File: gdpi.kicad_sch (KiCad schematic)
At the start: 20 parts, among them J7 HDMI_C_1.3, U1 ECP5U_12_CABGA256, U9 PCA9306DC1

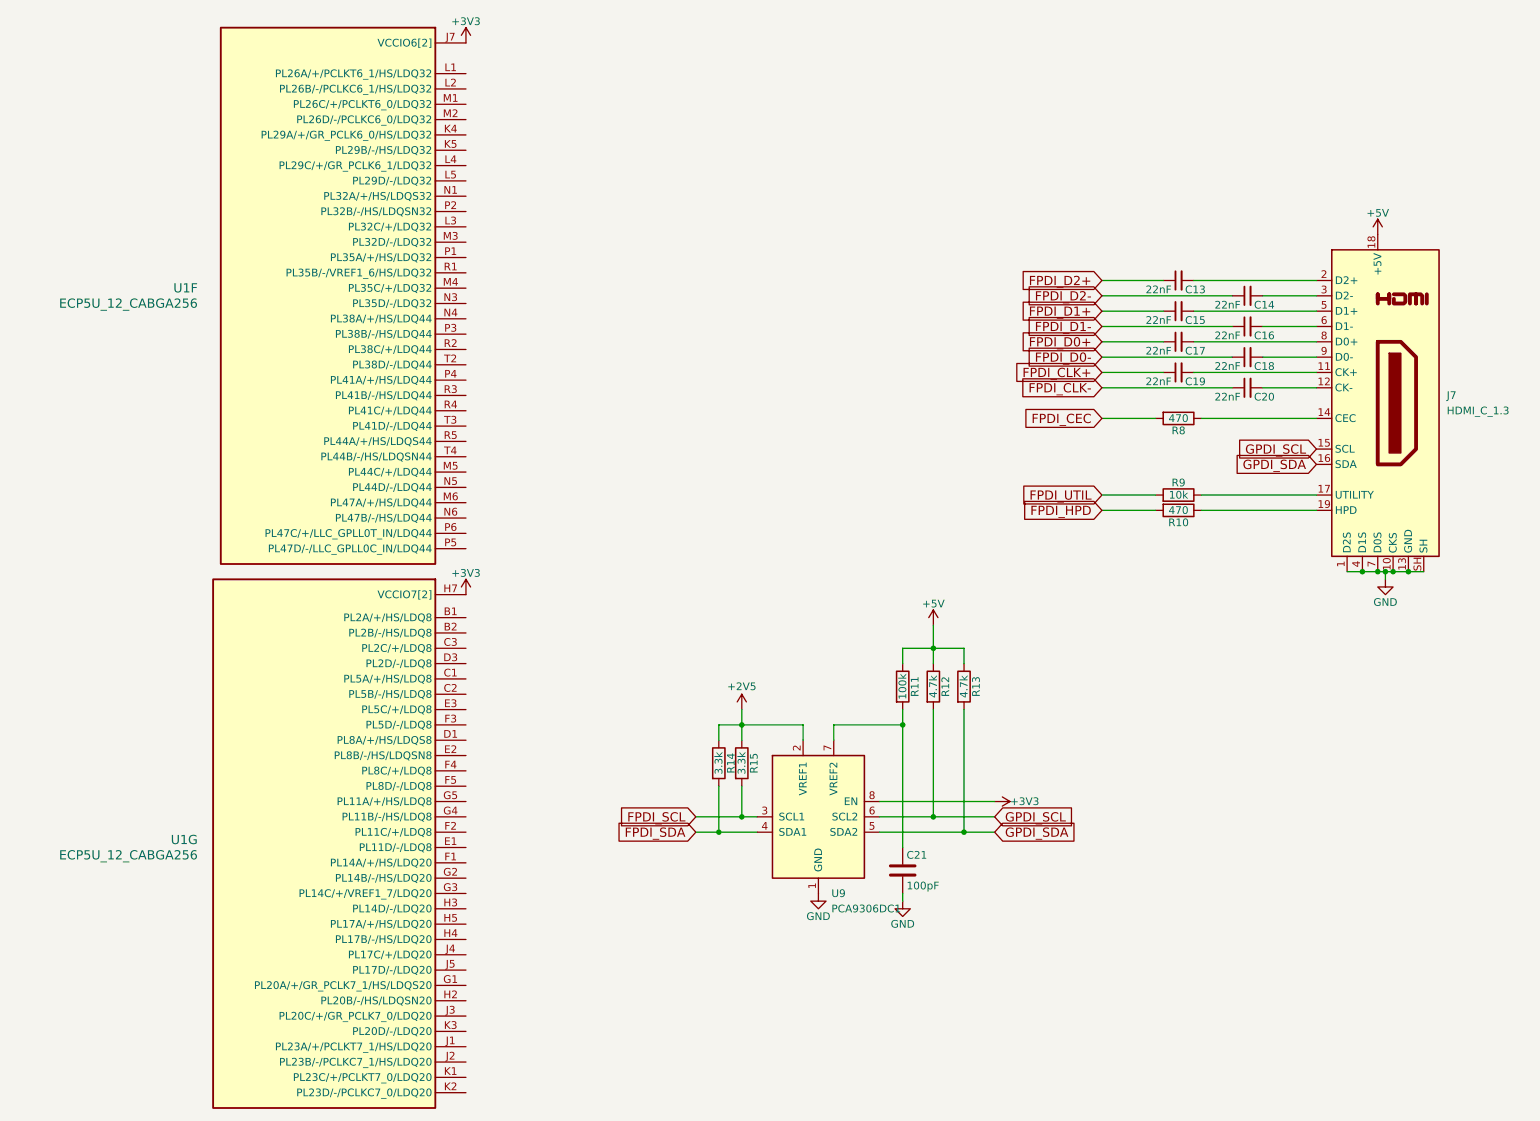
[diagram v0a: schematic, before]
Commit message: Routed HDMI, usb, rotated chip and more
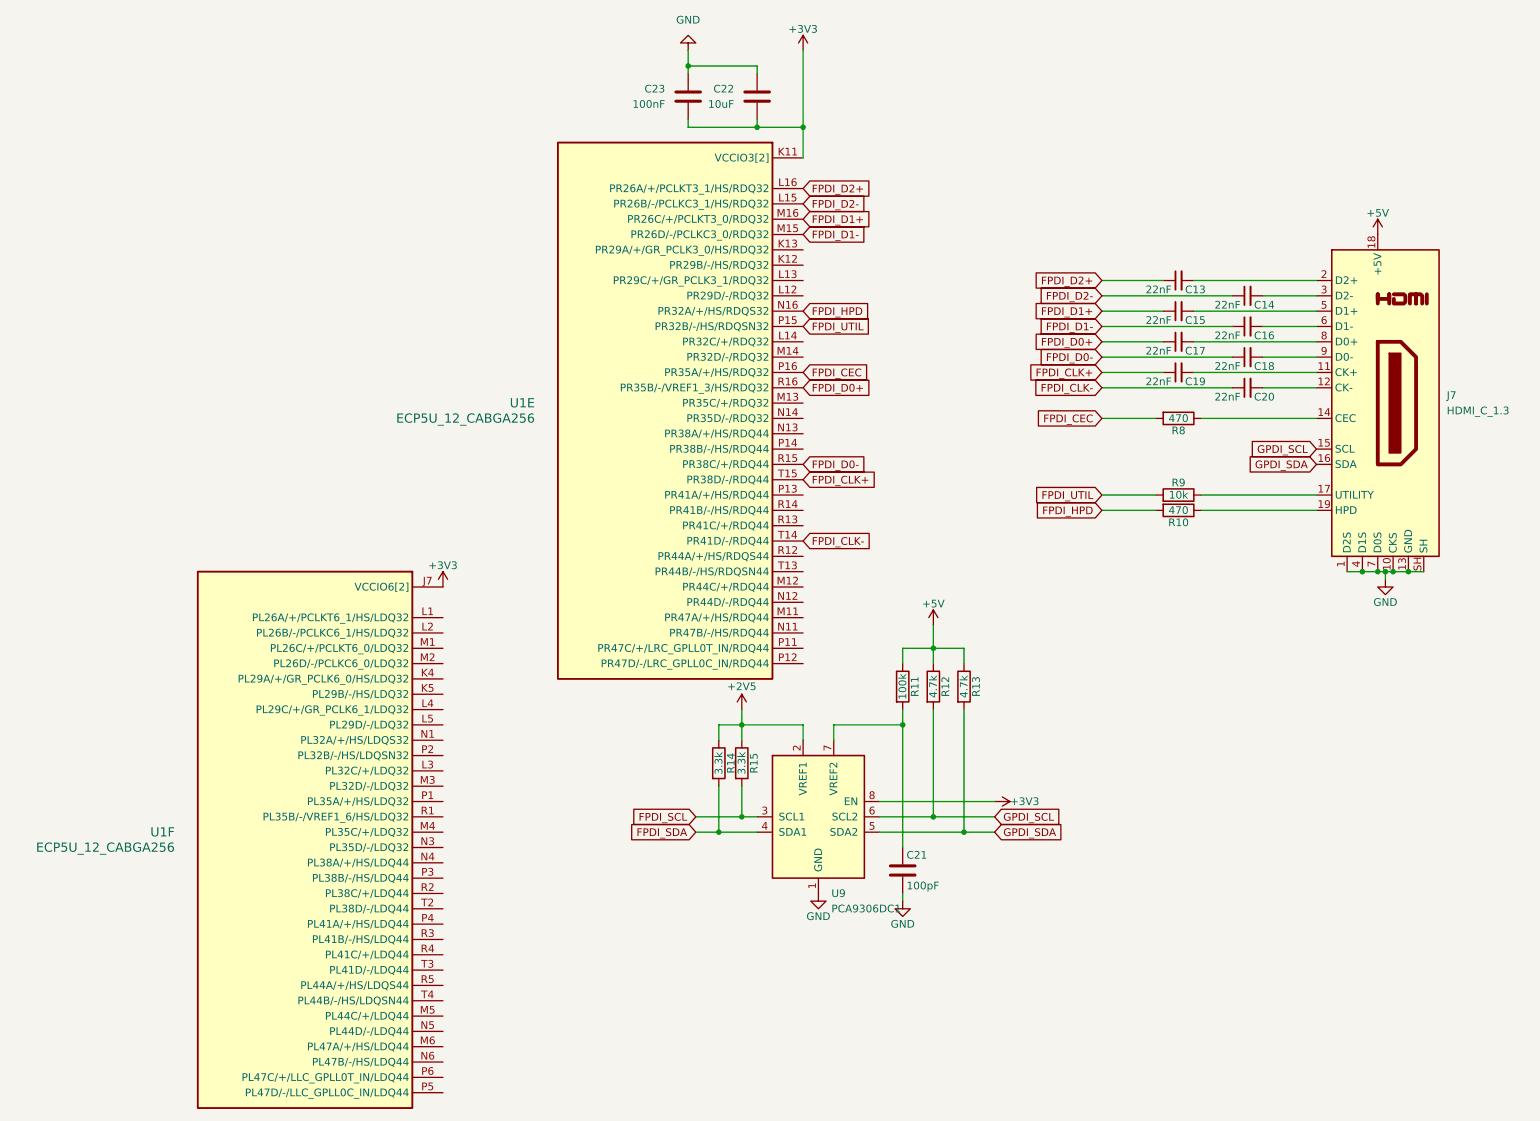
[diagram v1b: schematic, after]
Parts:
- removed unit 7 of U1
- added C22: 10uF, Capacitor_SMD:C_0603_1608Metric, symbol Device:C
- added C23: 100nF, Capacitor_SMD:C_0402_1005Metric, symbol Device:C
- added unit 5 of U1
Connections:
- net +3V3: now also C22.2, C23.2, U1.K11 (VCCIO3[2]), U1.L11 (VCCIO3[2])
- net FPDI_CEC: now also U1.P16 (PR35A/+/HS/RDQ32)
- net FPDI_CLK+: now also U1.T15 (PR38D/-/RDQ44)
- net FPDI_CLK-: now also U1.T14 (PR41D/-/RDQ44)
- net FPDI_D0+: now also U1.R16 (PR35B/-/VREF1_3/HS/RDQ32)
- net FPDI_D0-: now also U1.R15 (PR38C/+/RDQ44)
- net FPDI_D1+: now also U1.M16 (PR26C/+/PCLKT3_0/RDQ32)
- net FPDI_D1-: now also U1.M15 (PR26D/-/PCLKC3_0/RDQ32)
- net FPDI_D2+: now also U1.L16 (PR26A/+/PCLKT3_1/HS/RDQ32)
- net FPDI_D2-: now also U1.L15 (PR26B/-/PCLKC3_1/HS/RDQ32)
- net FPDI_HPD: now also U1.N16 (PR32A/+/HS/RDQS32)
- net FPDI_UTIL: now also U1.P15 (PR32B/-/HS/RDQSN32)
- net GND: now also C22.1, C23.1
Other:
- moved on the sheet: U1F

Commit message: Stash
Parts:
- removed C22: 10uF, Capacitor_SMD:C_0603_1608Metric, symbol Device:C
- removed unit 6 of U1
- added C39: 100nF, Capacitor_SMD:C_0402_1005Metric, symbol Device:C
- added C40: 15pF, Capacitor_SMD:C_0402_1005Metric, symbol Device:C
- added Y1: ECS-2520MV-xxx-xx, Crystal:Crystal_SMD_3225-4Pin_3.2x2.5mm, symbol Oscillator:ECS-2520MV-xxx-xx
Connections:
- net +2V5 is gone; now on net +3V3: R14.1, R15.1, U9.2 (VREF1)
- net +3V3: now also C39.1, Y1.1 (Tri-State), Y1.4 (VDD)
- net GND: now also C39.2, C40.2, Y1.2 (GND)
- net GCLK: now reaches U1.K13 (PR29A/+/GR_PCLK3_0/HS/RDQ32)
- net GCLK: now also C40.1, Y1.3 (OUT)
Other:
- moved on the sheet: C23, U1E

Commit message: Rev 1
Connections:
- net FPDI_CEC: now also U1.R12 (PR44A/+/HS/RDQS44); no longer U1.P16 (PR35A/+/HS/RDQ32)
- net FPDI_CLK-: now also U1.R15 (PR38C/+/RDQ44); no longer U1.T14 (PR41D/-/RDQ44)
- net FPDI_D0+: now also U1.P16 (PR35A/+/HS/RDQ32); no longer U1.R16 (PR35B/-/VREF1_3/HS/RDQ32)
- net FPDI_D0-: now also U1.R16 (PR35B/-/VREF1_3/HS/RDQ32); no longer U1.R15 (PR38C/+/RDQ44)

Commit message: No DRC Errors
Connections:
- net FPDI_CEC: now also U1.T14 (PR41D/-/RDQ44); no longer U1.R12 (PR44A/+/HS/RDQS44)
